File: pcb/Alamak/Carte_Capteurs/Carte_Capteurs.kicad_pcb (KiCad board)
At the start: 2 copper layers, 129.9 x 60 mm, 52 parts, among them J10 DF3A-5P-2DS, J11 DF3A-4P-2DS, J12 DF3A-4P-2DS, J13 Conn_01x02, J14 Conn_02x05_Odd_Even, J5 Conn_02x07_Odd_Even, J6 Molex KK 254, J7 Samtec FTS-105-01-L-DV, J8 Samtec FTS-105-01-L-DV, J9 DF3A-5P-2DS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

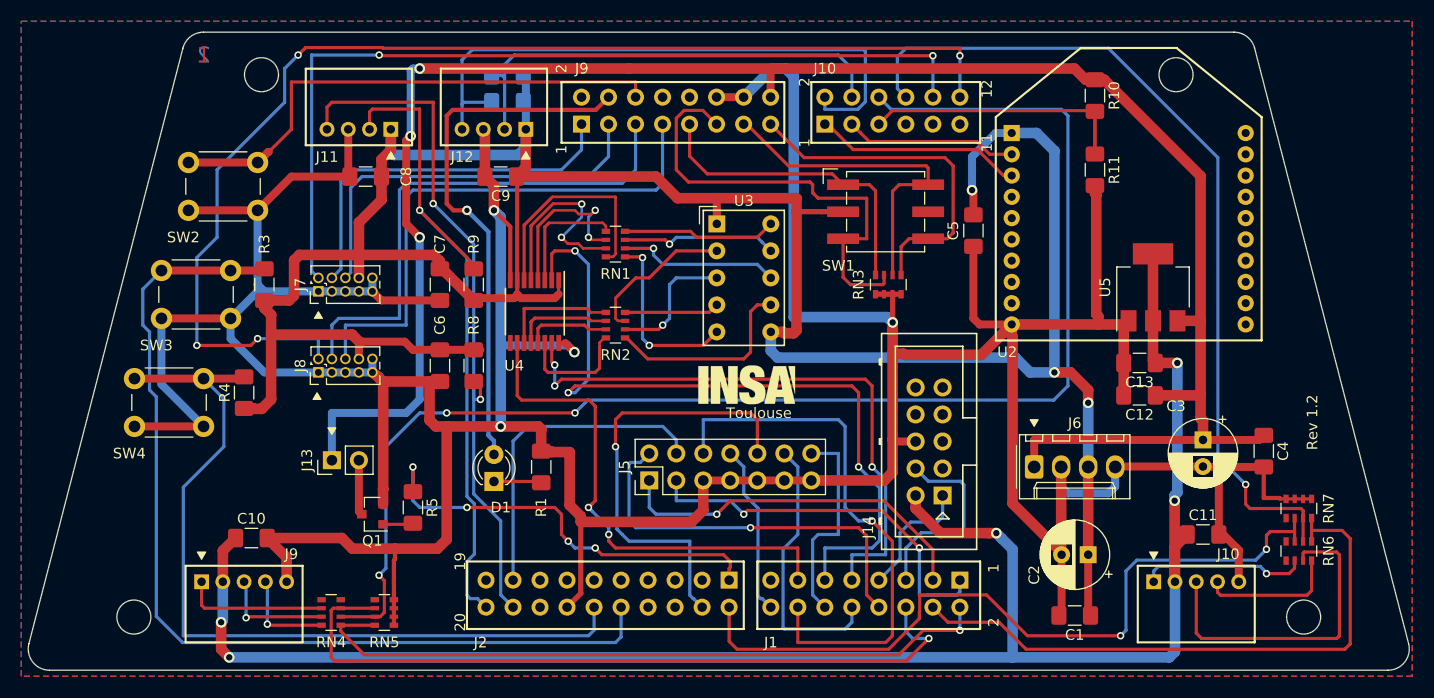
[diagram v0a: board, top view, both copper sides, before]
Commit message: Ajout des regles NXP Cup pour 2020 (V1) + modifs mineures sur pcbs
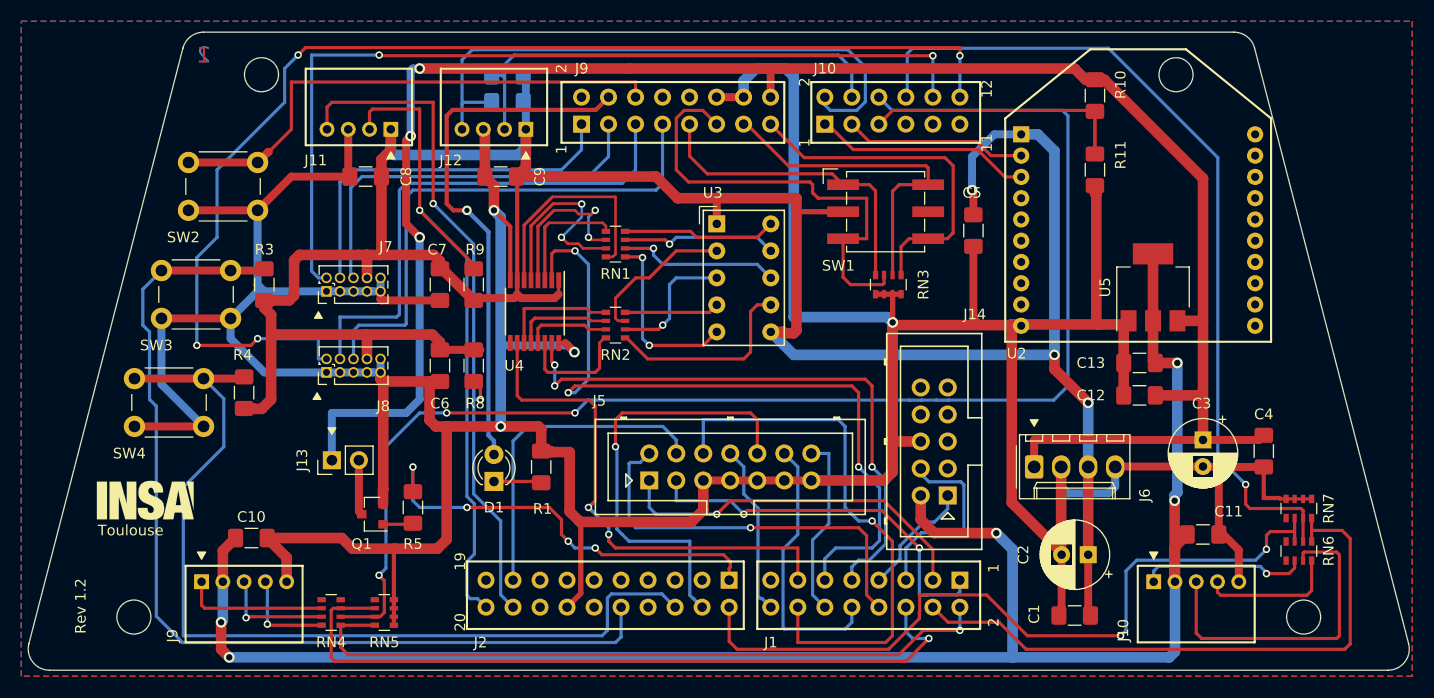
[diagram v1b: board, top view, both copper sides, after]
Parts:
- J5: footprint Connector_PinHeader_2.54mm:PinHeader_2x07_P2.54mm_Vertical -> Connector_Multicomp:Multicomp_MC9A12-1434_2x07_P2.54mm_Vertical
- moved Logo1 57.6 mm to (98.2, 110.6)
- moved U2 0.90 mm to (191.4, 82.0)
- moved J7 0.76 mm to (115.1, 90.8)
- moved J8 0.76 mm to (115.1, 98.4)
- moved J14 0.48 mm to (173.5, 110.0)
- turned J5 to 0 degrees
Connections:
- U1 pad 2.12: /SW_USER2 -> (no net)
- U1 pad 2.6: (no net) -> /SW_USER2
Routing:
- net /SW_USER2: track 77.9 -> 87.1 mm
- net GND: track 463.0 -> 466.5 mm
- net +3V3: track 263.0 -> 260.0 mm
- net /PWM_MOT_R_2: track 19.6 -> 17.2 mm
- net /DISP_CLK: track 56.5 -> 55.2 mm
- net /CCD_CLK1: track 51.2 -> 50.0 mm
- net /ENC_SIG_A2: track 81.1 -> 80.0 mm
- net /SENS_SCL2: track 57.8 -> 56.7 mm
- net /USART_TX: track 19.6 -> 20.5 mm
- net /USART_RX: track 16.2 -> 17.2 mm
- net /ENC_SIG_B1: track 66.0 -> 66.9 mm
- net /CCD_AD1: track 112.0 -> 112.8 mm
- net /CCD_AD0: track 83.6 -> 84.3 mm
- net /PIXY2_RX: track 11.9 -> 11.2 mm
- net /DISP_SIN: track 70.8 -> 70.2 mm
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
